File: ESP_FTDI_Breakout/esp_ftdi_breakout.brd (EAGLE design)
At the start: 50.8 x 25.1 mm, 3 parts

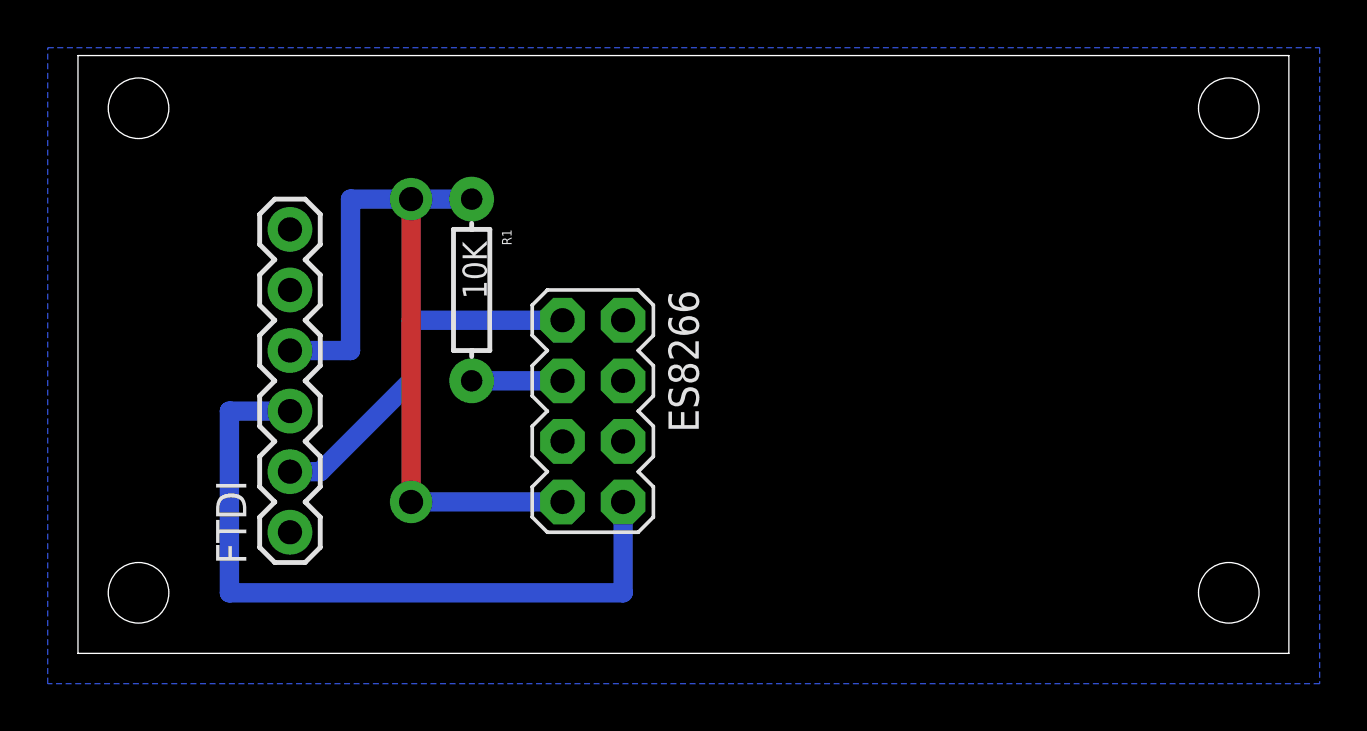
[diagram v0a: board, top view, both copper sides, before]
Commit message: Added switch to ESP_FTDI_BREAKOUT
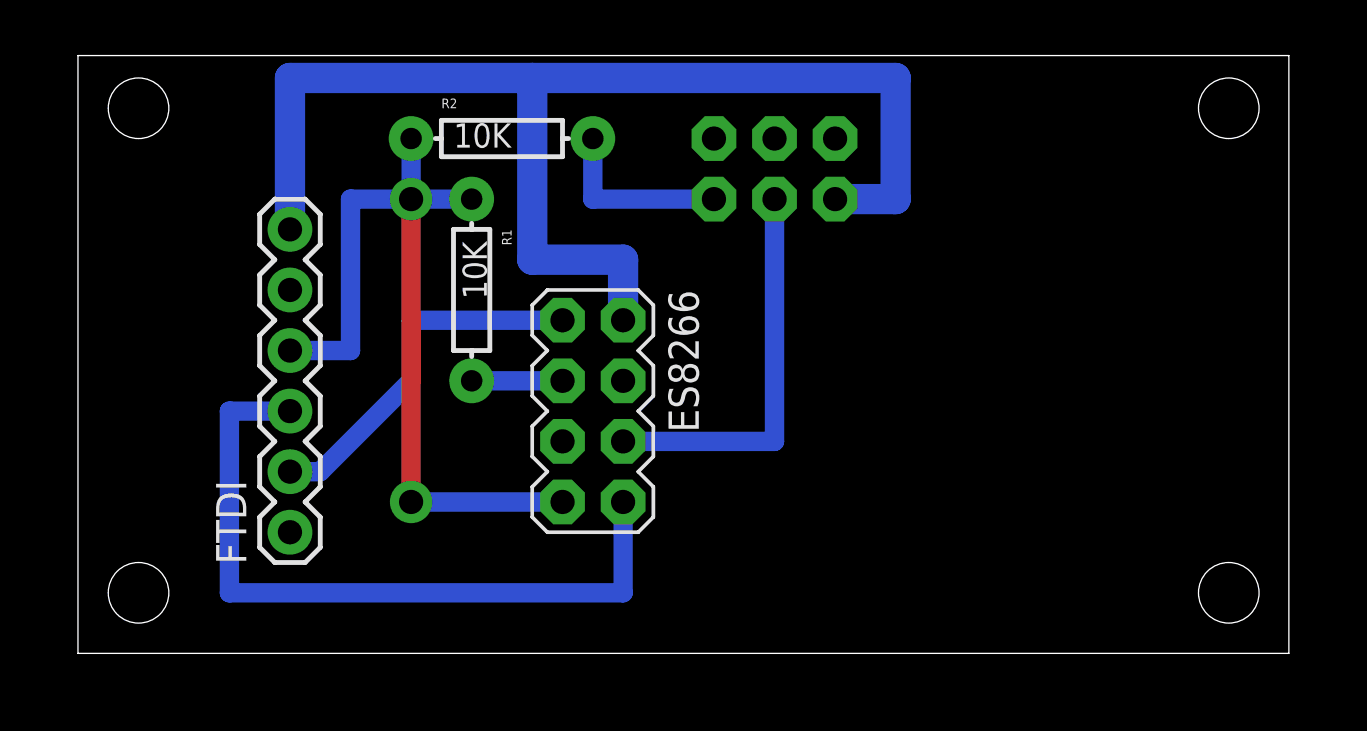
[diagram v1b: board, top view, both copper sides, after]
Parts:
- added R2: 10K, SparkFun-Resistors:AXIAL-0.3
- added SWITCH1: SWITCH, SparkFun-Connectors:2X3
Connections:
- new net GPIO0: ES8266.6, SWITCH1.4
- new net N$2: R2.P$2, SWITCH1.2
- net GND: now also SWITCH1.6; no longer ES8266.6
- net VCC: now also R2.P$1
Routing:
- net GND: track 0.00 -> 53.3 mm
- net GPIO0: track 0.00 -> 16.5 mm
- net N$2: track 0.00 -> 7.62 mm
- net VCC: track 33.0 -> 35.6 mm
- removed copper zone on layer 16, net GND
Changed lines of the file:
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@@
 <attribute name="PROD_ID" value="RES-12182" x="16.51" y="15.24" size="1.778" layer="27" rot="R270" display="off"/>
+</element>
+<element name="SWITCH1" library="SparkFun-Connectors" package="2X3" value="SWITCH" x="26.67" y="21.59" rot="MR180">
+<attribute name="PROD_ID" value="CONN-11566" x="26.67" y="21.59" size="1.778" layer="28" rot="MR180" display="off"/>
+</element>
+<element name="R2" library="SparkFun-Resistors" package="AXIAL-0.3" value="10K" x="17.78" y="21.59">
+<attribute name="PROD_ID" value="RES-12182" x="17.78" y="21.59" size="1.778" layer="27" display="off"/>
 </element>
 </elements>
@@
 <contactref element="FTDI" pad="6"/>
 <contactref element="ES8266" pad="2"/>
-<contactref element="ES8266" pad="6"/>
-<polygon width="0.1524" layer="16">
-<vertex x="-1.27" y="-1.27"/>
-<vertex x="-1.27" y="25.4"/>
-<vertex x="52.07" y="25.4"/>
-<vertex x="52.07" y="-1.27"/>
-</polygon>
+<contactref element="SWITCH1" pad="6"/>
+<wire x1="8.89" y1="17.78" x2="8.89" y2="24.13" width="1.27" layer="16"/>
+<wire x1="34.29" y1="24.13" x2="34.29" y2="19.05" width="1.27" layer="16"/>
+<wire x1="34.29" y1="19.05" x2="31.75" y2="19.05" width="1.27" layer="16"/>
+<wire x1="19.05" y1="24.13" x2="8.89" y2="24.13" width="1.27" layer="16"/>
+<wire x1="19.05" y1="24.13" x2="34.29" y2="24.13" width="1.27" layer="16"/>
+<wire x1="22.86" y1="13.97" x2="22.86" y2="16.51" width="1.27" layer="16"/>
+<wire x1="22.86" y1="16.51" x2="19.05" y2="16.51" width="1.27" layer="16"/>
+<wire x1="19.05" y1="16.51" x2="19.05" y2="24.13" width="1.27" layer="16"/>
 </signal>
 <signal name="CTS">
@@
 <wire x1="11.43" y1="12.7" x2="11.43" y2="19.05" width="0.8128" layer="16"/>
 <wire x1="11.43" y1="19.05" x2="13.97" y2="19.05" width="0.8128" layer="16"/>
+<contactref element="R2" pad="P$1"/>
+<wire x1="13.97" y1="21.59" x2="13.97" y2="19.05" width="0.8128" layer="16"/>
 </signal>
 <signal name="TX">
@@
 <contactref element="ES8266" pad="4"/>
 </signal>
+<signal name="N$2">
+<contactref element="SWITCH1" pad="2"/>
+<contactref element="R2" pad="P$2"/>
+<wire x1="26.67" y1="19.05" x2="21.59" y2="19.05" width="0.8128" layer="16"/>
+<wire x1="21.59" y1="19.05" x2="21.59" y2="21.59" width="0.8128" layer="16"/>
+</signal>
+<signal name="GPIO0">
+<contactref element="ES8266" pad="6"/>
+<contactref element="SWITCH1" pad="4"/>
+<wire x1="22.86" y1="8.89" x2="29.21" y2="8.89" width="0.8128" layer="16"/>
+<wire x1="29.21" y1="8.89" x2="29.21" y2="19.05" width="0.8128" layer="16"/>
+</signal>
 </signals>
